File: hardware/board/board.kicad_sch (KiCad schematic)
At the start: 12 parts, among them J101 UART, J102 CM4_DEBUG, J103 DEBUG_PORT, U101 Oled

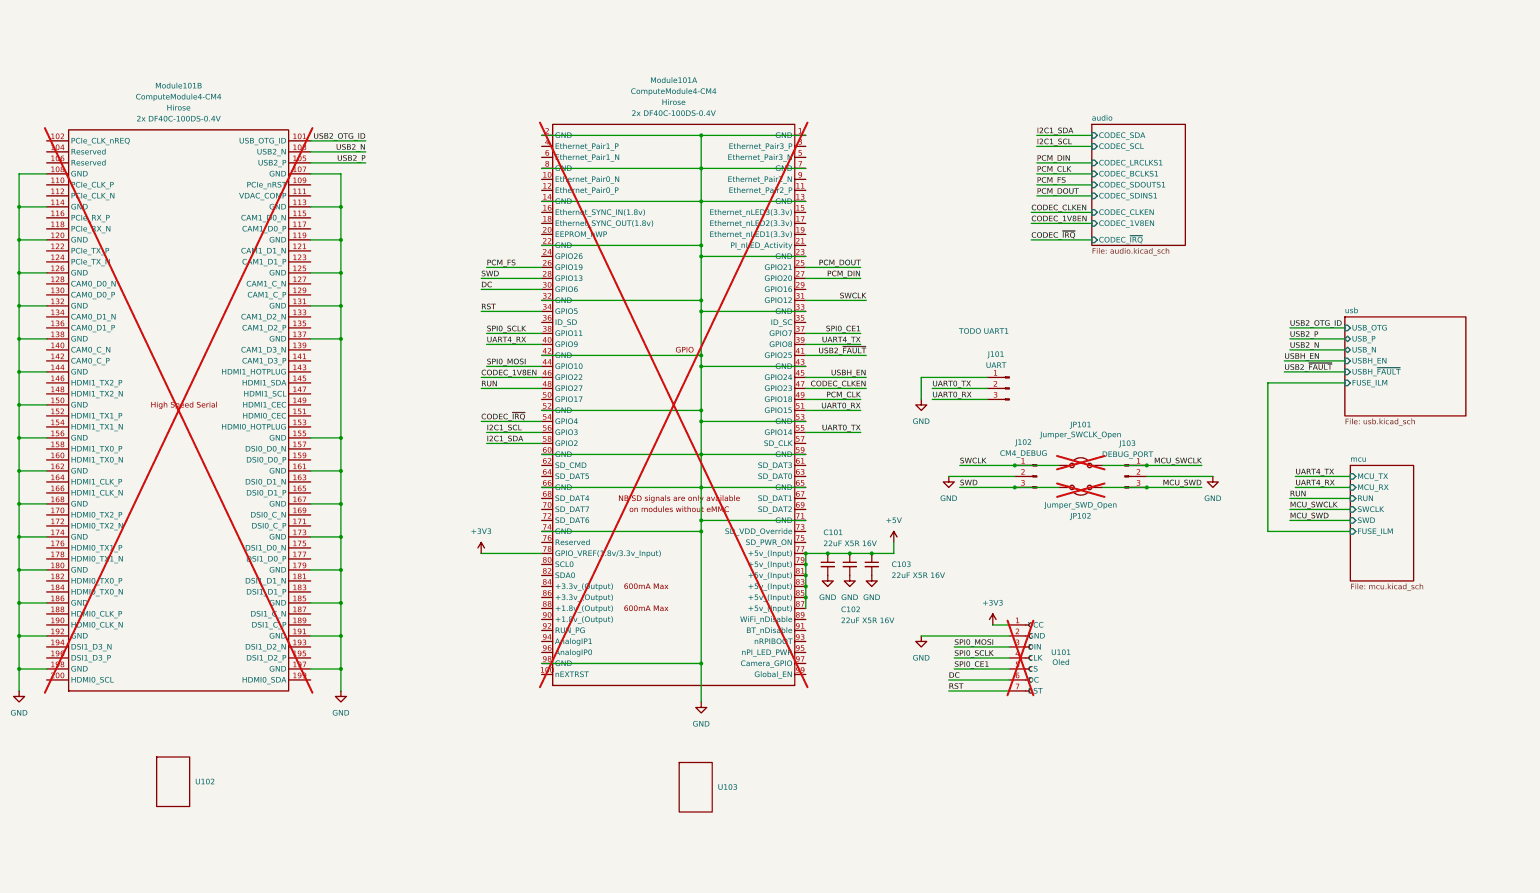
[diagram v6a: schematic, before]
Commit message: 3v3out, delete usb, add leds, LDO
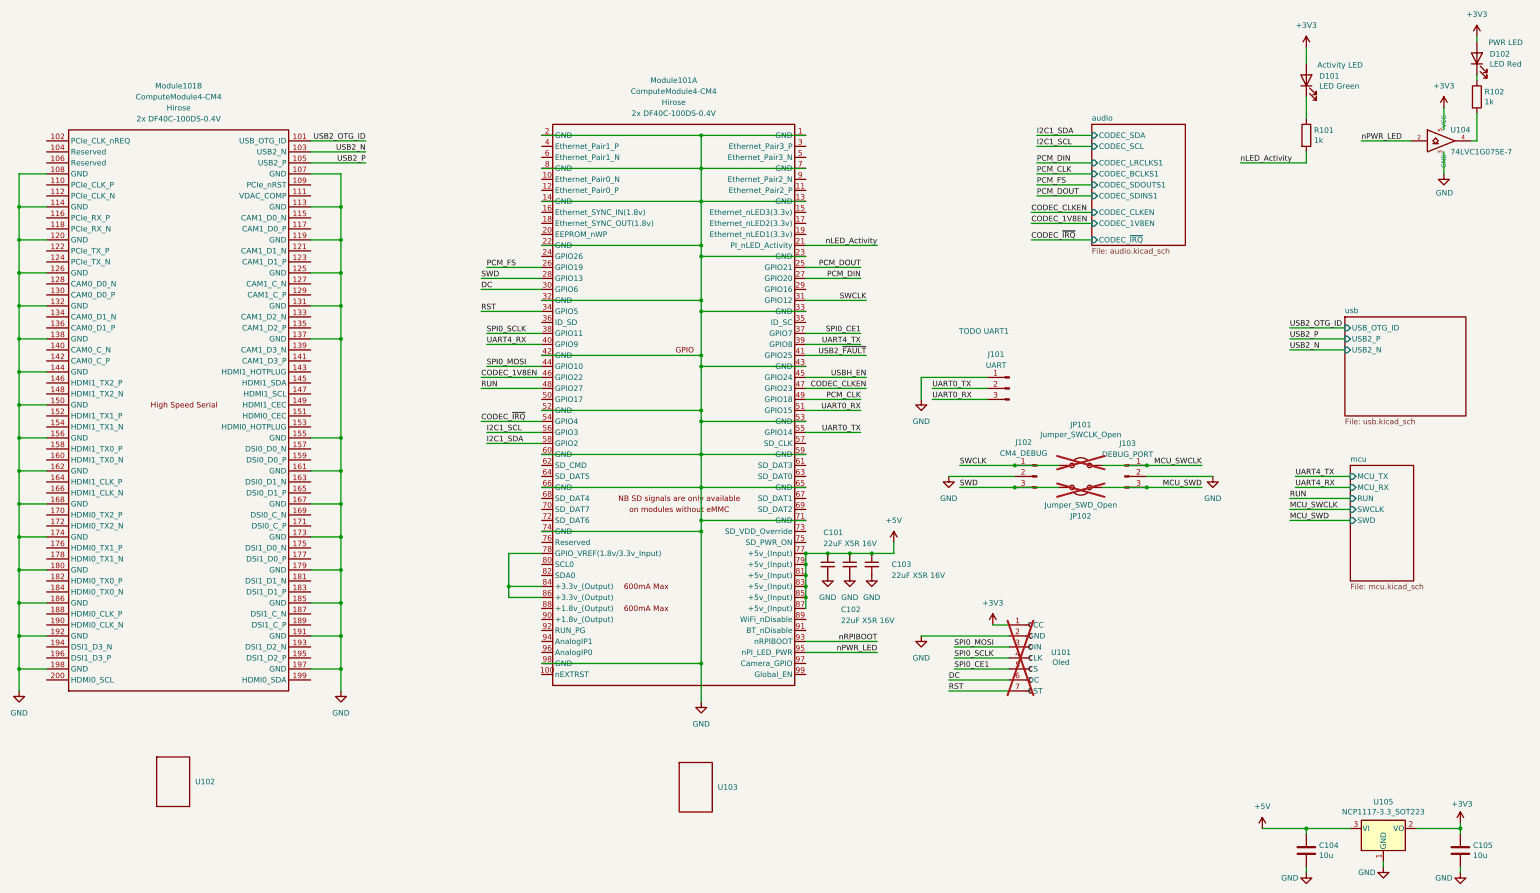
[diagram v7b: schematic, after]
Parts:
- added C104, C105: 10u, Capacitor_SMD:C_0805_2012Metric, symbol Device:C
- added D101: LED Green, LED_SMD:LED_0603_1608Metric, symbol Device:LED
- added D102: LED Red, LED_SMD:LED_0603_1608Metric, symbol Device:LED
- added R101, R102: 1k, Resistor_SMD:R_0603_1608Metric_Pad0.98x0.95mm_HandSolder, symbol Device:R
- added U104: 74LVC1G07SE-7, Package_TO_SOT_SMD:SOT-353_SC-70-5, symbol CM4IO:74LVC1G07_copy
- added U105: NCP1117-3.3_SOT223, Package_TO_SOT_SMD:SOT-223-3_TabPin2, symbol Regulator_Linear:NCP1117-3.3_SOT223
- Module101: now fitted
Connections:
- net +3V3: now also C105.1, D101.2 (A), D102.2 (A), U104.5 (VCC), U105.2 (VO); no longer Module101.78 (GPIO_VREF(1.8v/3.3v_Input))
- net +5V: now also C104.1, U105.3 (VI)
- net GND: now also C104.2, C105.2, U104.3 (GND), U105.1 (GND)
- net nLED_Activity: now reaches Module101.21 (PI_nLED_Activity)
- net nLED_Activity: now also R101.2
- net at Module101.84 (+3.3v_(Output)): now also Module101.78 (GPIO_VREF(1.8v/3.3v_Input)), Module101.86 (+3.3v_(Output))
- net nRPIBOOT: now reaches Module101.93 (nRPIBOOT)
- net nPWR_LED: now reaches Module101.95 (nPI_LED_PWR)
- net nPWR_LED: now also U104.2
- new net: D101.1 (K), R101.1
- new net: R102.2, U104.4
- new net: D102.1 (K), R102.1
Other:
- sheet mcu ports: added none; removed FUSE_ILM
- sheet usb ports: added USB2_N, USB2_P, USB_OTG_ID; removed FUSE_ILM, USBH_EN, USBH_~{FAULT}, USB_N, USB_OTG, USB_P
- note added: "Activity LED"
- note added: "PWR LED"

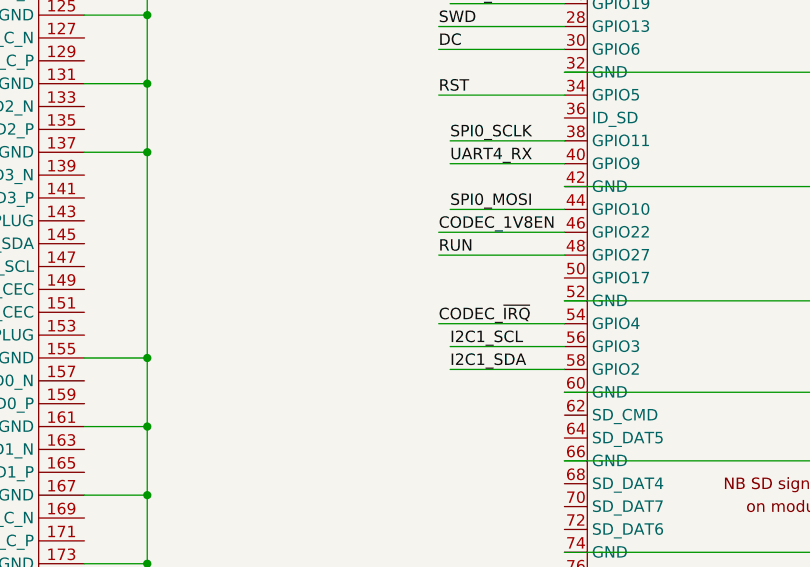
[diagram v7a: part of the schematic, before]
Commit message: i2c pullup
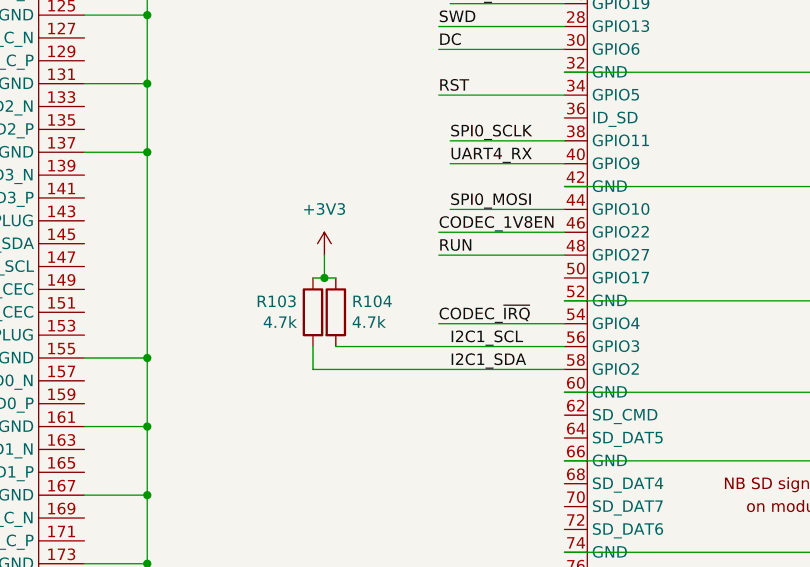
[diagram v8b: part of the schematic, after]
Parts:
- added R103, R104: 4.7k, Resistor_SMD:R_0603_1608Metric_Pad0.98x0.95mm_HandSolder, symbol Device:R
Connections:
- net +3V3: now also R103.1, R104.1
- net I2C1_SCL: now also R104.2
- net I2C1_SDA: now also R103.2
